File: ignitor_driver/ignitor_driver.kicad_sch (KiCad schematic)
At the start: 53 parts, among them J1 Conn_02x05_Counter_Clockwise, J2 24V_IN, J3 GND_IN, J4 Conn_02x01, K1 G5LE-1 DC24, K2 G5LE-1 DC24, K3 G5LE-1 DC24, Q1 PMOS, Q2 BSS138, Q3 BSS138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

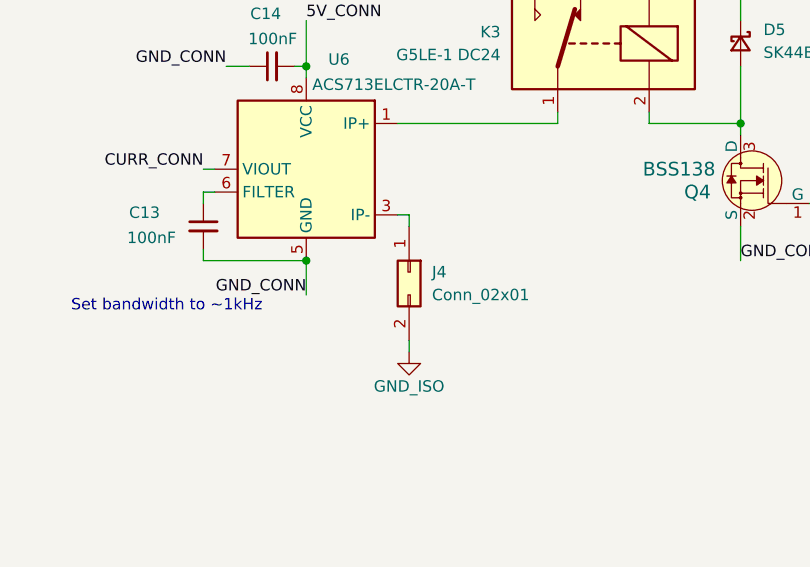
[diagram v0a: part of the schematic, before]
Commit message: finish ignitor board routing
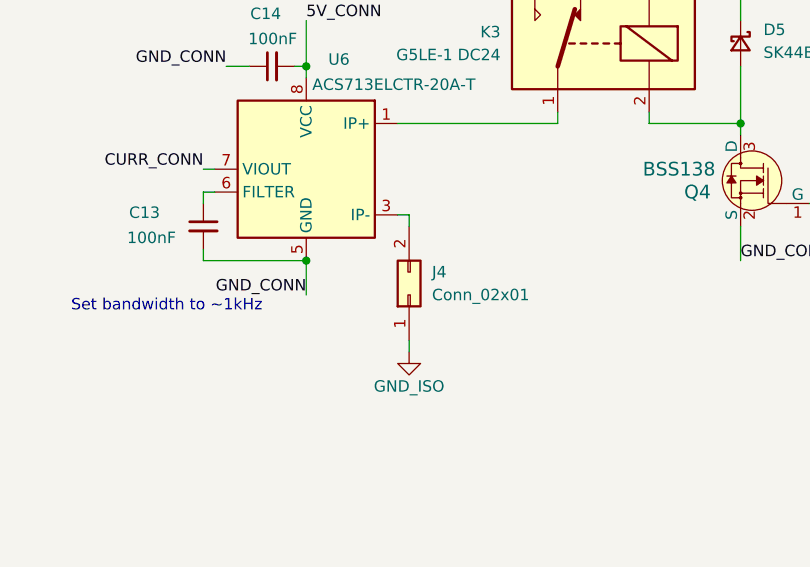
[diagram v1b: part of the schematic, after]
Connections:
- net GND_ISO: now also J4.1 (Pin_1); no longer J4.2 (Pin_2)
- net at U6.3 (IP-), U6.4 (IP-): now also J4.2 (Pin_2); no longer J4.1 (Pin_1)
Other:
- moved on the sheet: J4
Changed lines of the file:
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@@
 	(symbol
 		(lib_id "Connector_Generic:Conn_02x01")
-		(at 209.55 149.86 270)
+		(at 209.55 152.4 90)
 		(unit 1)
 		(body_style 1)
@@
 					(size 1.27 1.27)
 				)
-				(justify left)
+				(justify right)
 			)
 		)
@@
 					(size 1.27 1.27)
 				)
-				(justify left)
+				(justify right)
 			)
 		)
 		(property "Footprint" "Connector_Molex:Molex_Mini-Fit_Jr_5566-02A_2x01_P4.20mm_Vertical"
-			(at 209.55 149.86 0)
+			(at 209.55 152.4 0)
 			(hide yes)
 			(show_name no)
@@
 		)
 		(property "Datasheet" ""
-			(at 209.55 149.86 0)
+			(at 209.55 152.4 0)
 			(hide yes)
 			(show_name no)
@@
 		)
 		(property "Description" "Generic connector, double row, 02x01, this symbol is compatible with counter-clockwise, top-bottom and odd-even numbering schemes., script generated (kicad-library-utils/schlib/autogen/connector/)"
-			(at 209.55 149.86 0)
+			(at 209.55 152.4 0)
 			(hide yes)
 			(show_name no)

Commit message: updates for manufacturing
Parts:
- C5: now left out of the parts list
- F1: LCSC N/A -> (none)
- Q2, Q3, Q4: Description_1 MOSFET N-CH 50V 220MA SOT-23 -> (none)
- R1, R11, R2, R4, R6, R8, R9: LCSC C25076 -> (none)
- R10, R12, R13: LCSC C25531 -> (none)
- R3: value 10k -> 10k 0.1%; LCSC C25076 -> (none)
- R5: value 30k -> 30k 0.1%; LCSC C25076 -> (none)
- R7: footprint Resistor_SMD:R_0805_2012Metric_Pad1.20x1.40mm_HandSolder -> Resistor_SMD:R_0603_1608Metric_Pad0.98x0.95mm_HandSolder; LCSC C25076 -> (none)
- U6: value ACS713ELCTR-20A-T -> ACS724xLCTR-30AU; symbol Sensor_Current:ACS713xLCTR-20A -> Sensor_Current:ACS724xLCTR-30AU; MPN ACS713ELCTR-20A-T -> ACS724LLCTR-30AU-T
